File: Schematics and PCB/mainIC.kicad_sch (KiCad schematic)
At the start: 46 parts, among them J1 ICSP, Q1 FDN340P, SW1 RESET_SW, U1 ATmega32U4, U2 NCP1117ST50T3G, U3 LMV358IDGKR, U4 LP2985-33DBVR, Y1 16MHz 20pF GND24

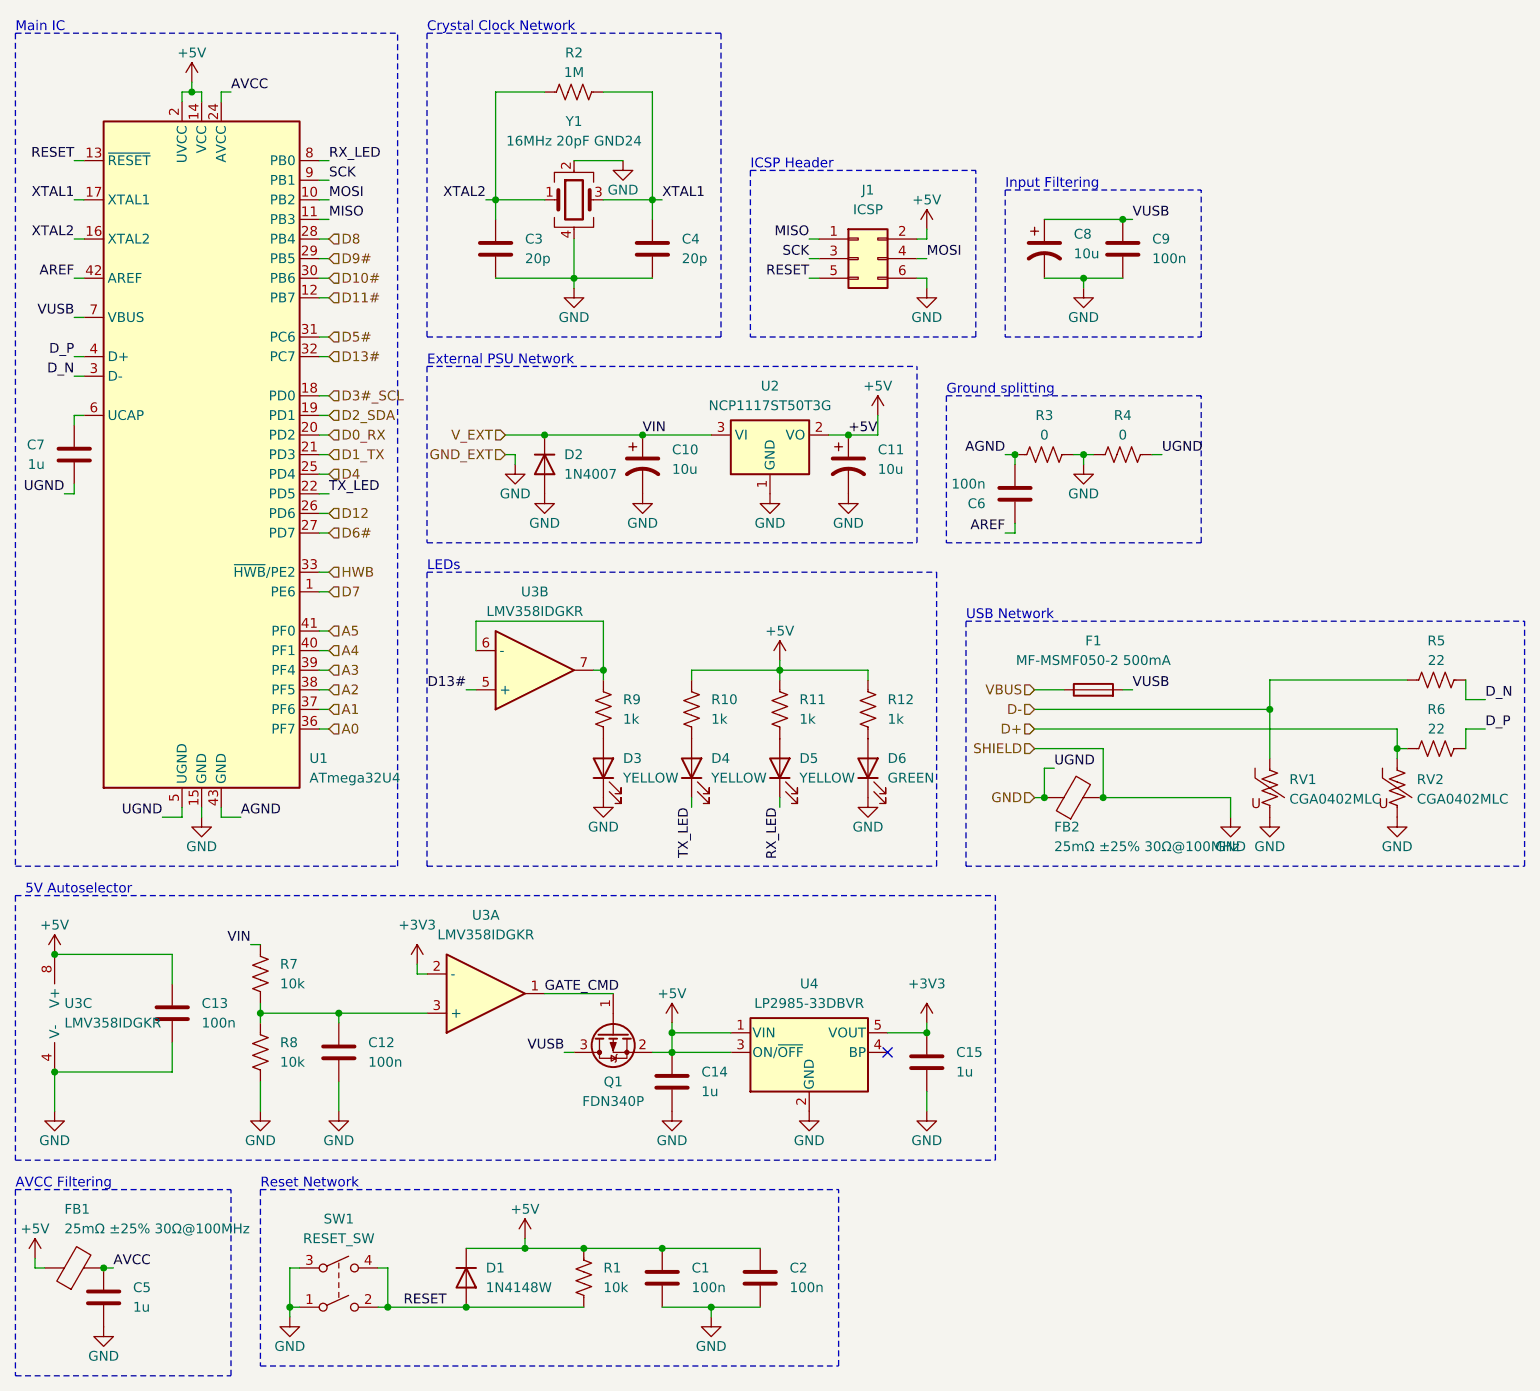
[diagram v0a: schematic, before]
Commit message: schematic progress
added li-po charge circuits and usb hub
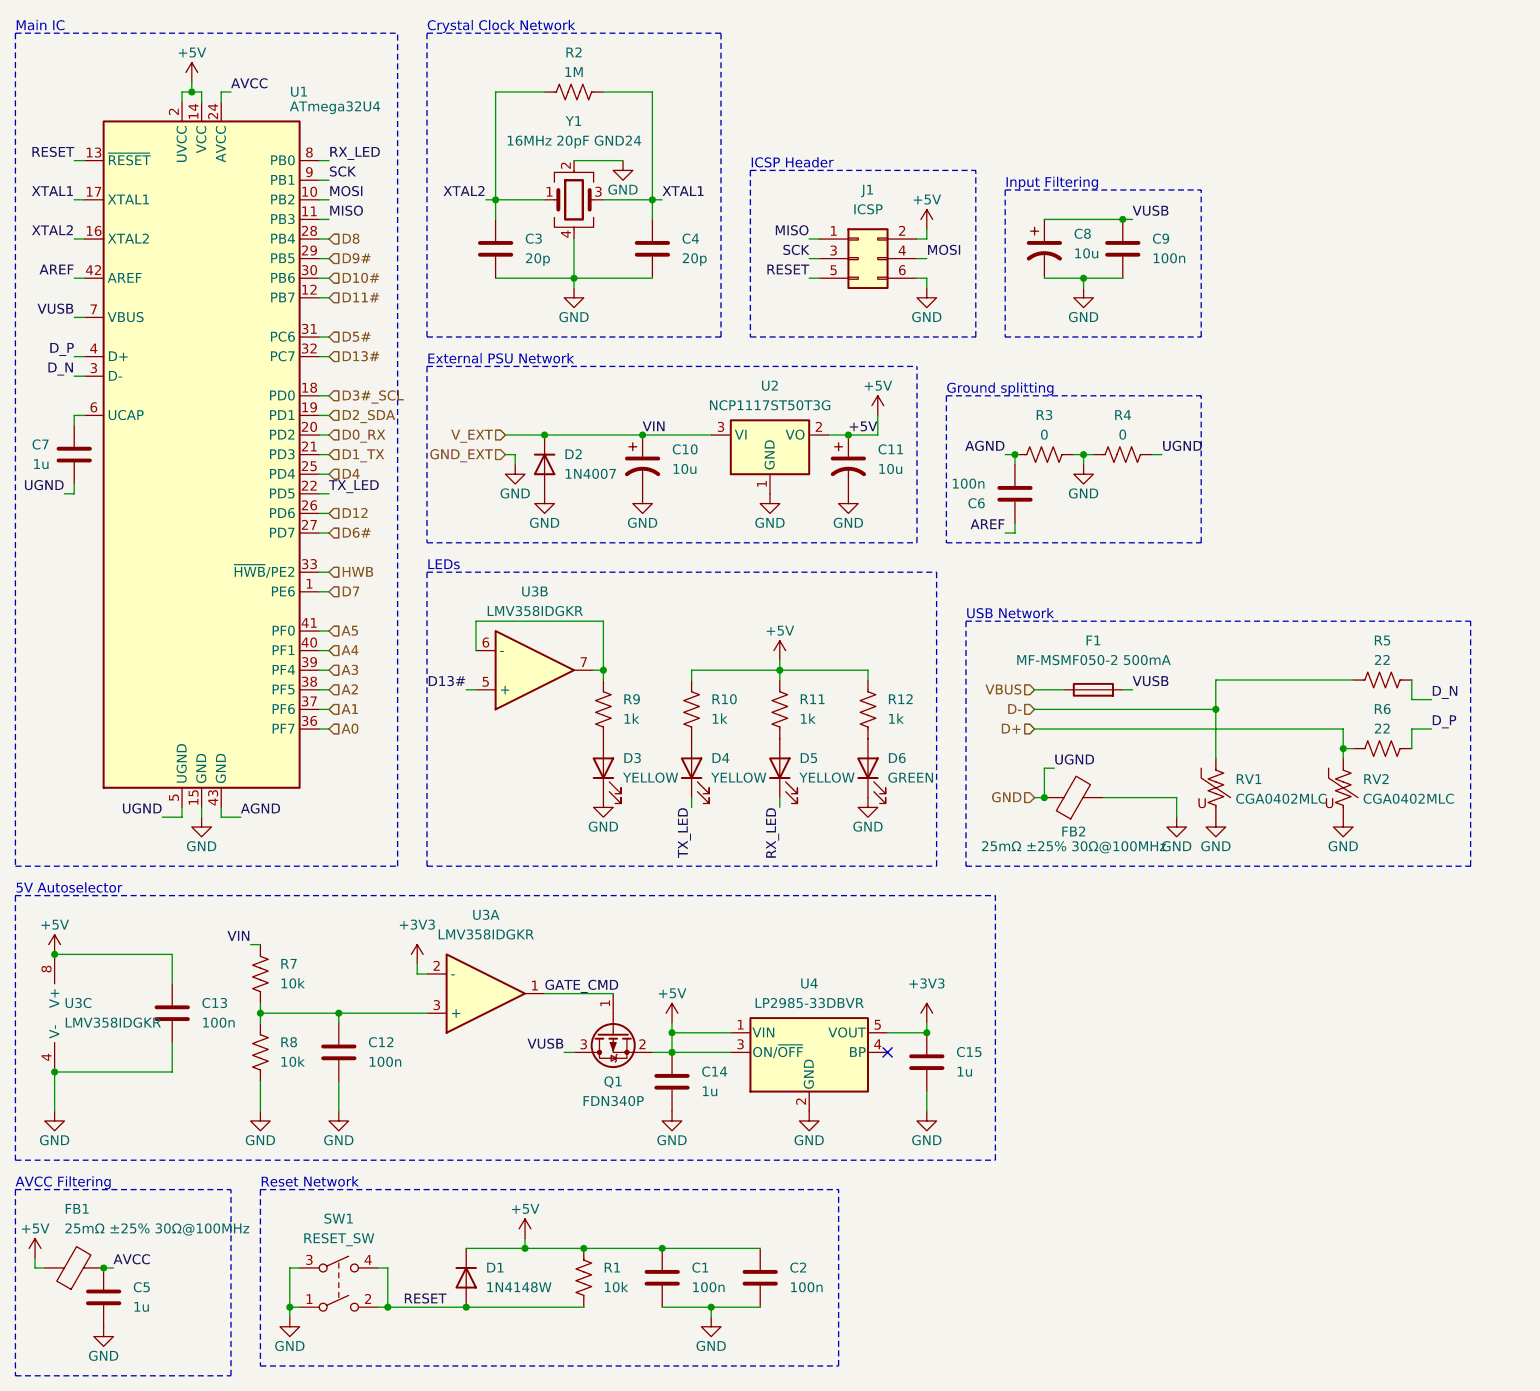
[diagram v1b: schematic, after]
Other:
- moved on the sheet: R5, R6, RV1, RV2

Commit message: Updated USB hub
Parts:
- R2: footprint (none) -> Resistor_SMD:R_0603_1608Metric
